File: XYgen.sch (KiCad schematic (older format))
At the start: 24 parts, among them J1 V_analog_in, J10 Mounting Hole, J11 Mounting Hole, J12 Mounting Hole, J13 Mounting Hole, J2 Ones, J3 Tens, J4 Hundreds, J5 Thousands, J6 Vin, J7 Blanking, J8 XOut, J9 YOut, U1 40106, U2 74HC123, U3 74HC08, U4 74HC32

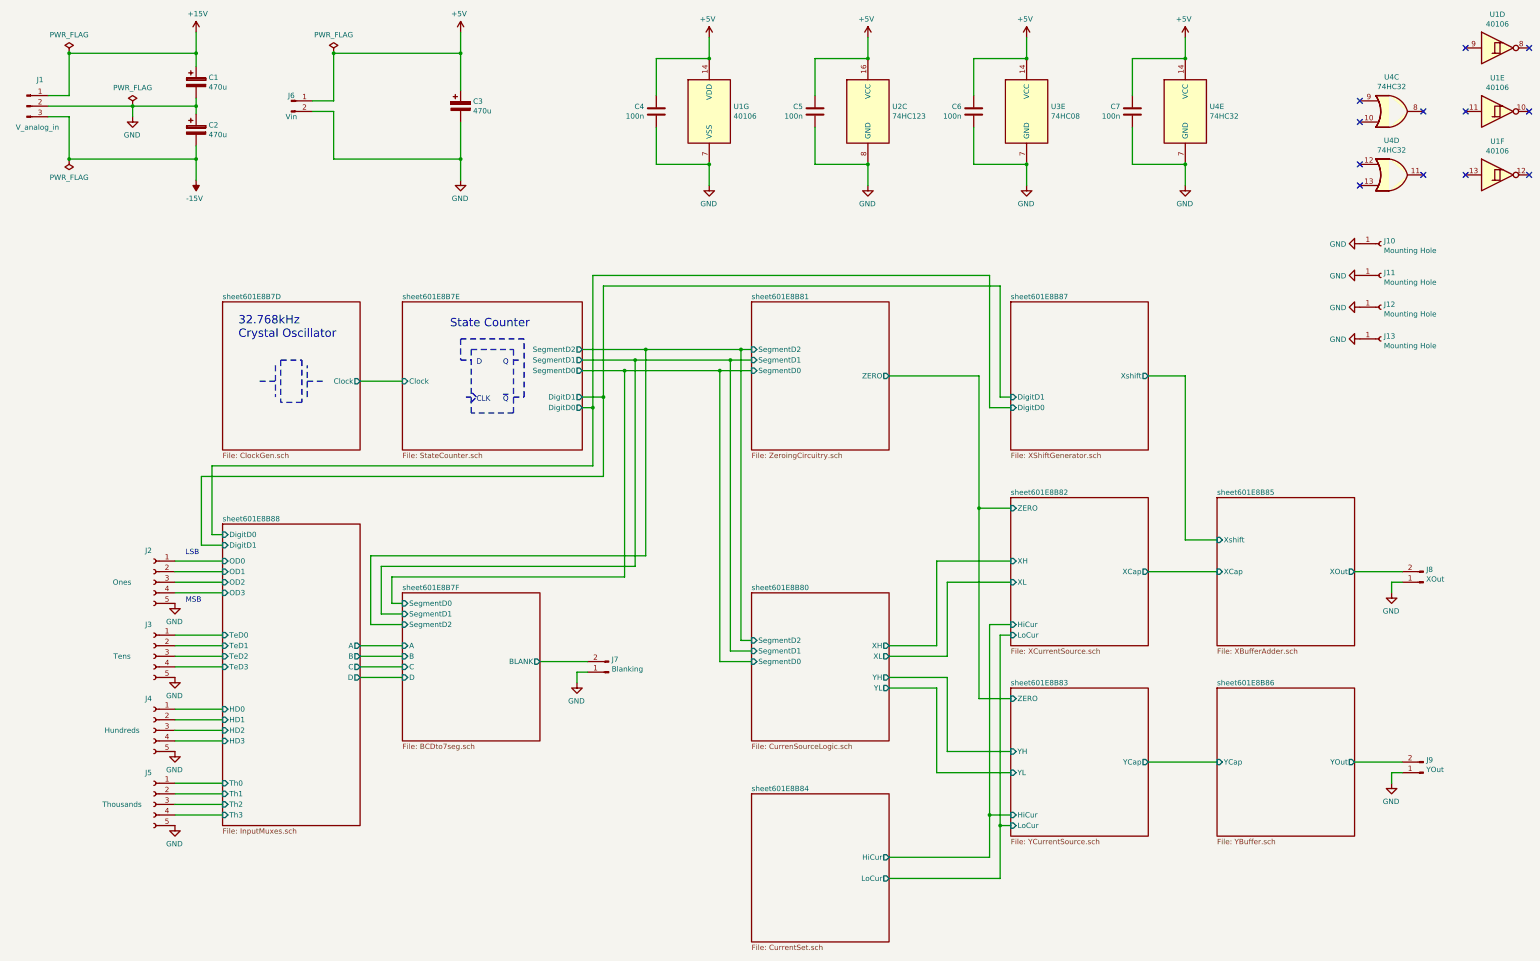
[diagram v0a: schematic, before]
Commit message: Fixed some bugs, finished block symbols
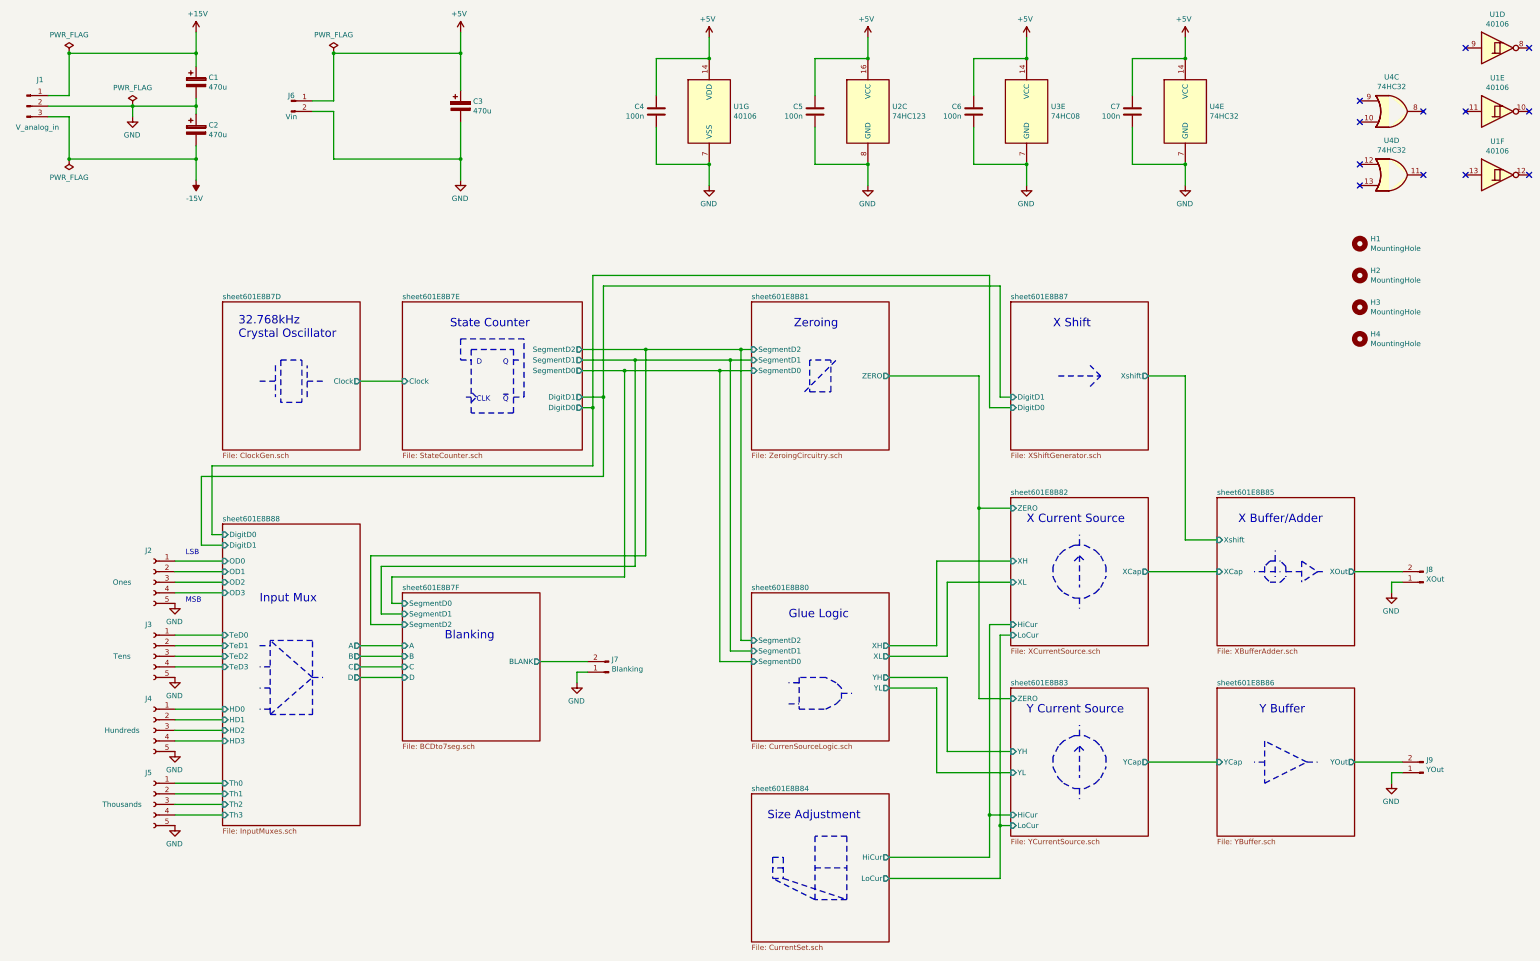
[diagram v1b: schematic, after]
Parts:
- removed J10, J11, J12, J13: Mounting Hole, MountingHole:MountingHole_3.2mm_M3_Pad, symbol Connector:Conn_01x01_Female
- added H1, H2, H3, H4: MountingHole, MountingHole:MountingHole_2.7mm_M2.5, symbol Mechanical:MountingHole
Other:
- note added: "Blanking"
- note added: "Glue Logic"
- note added: "Input Mux"
- note added: "Size Adjustment"
- note added: "X Buffer/Adder"
- note added: "X Current Source"
- note added: "X Shift"
- note added: "Y Buffer"
- note added: "Y Current Source"
- note added: "Zeroing"
